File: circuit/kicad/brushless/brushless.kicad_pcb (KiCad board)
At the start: 2 copper layers, 52.3 x 51.5 mm, 20 parts, among them J1 MOTOR_OUTPUT, J2 POWER_INPUT, Q1 IRF540N, Q2 IRF540N, Q3 IRF540N

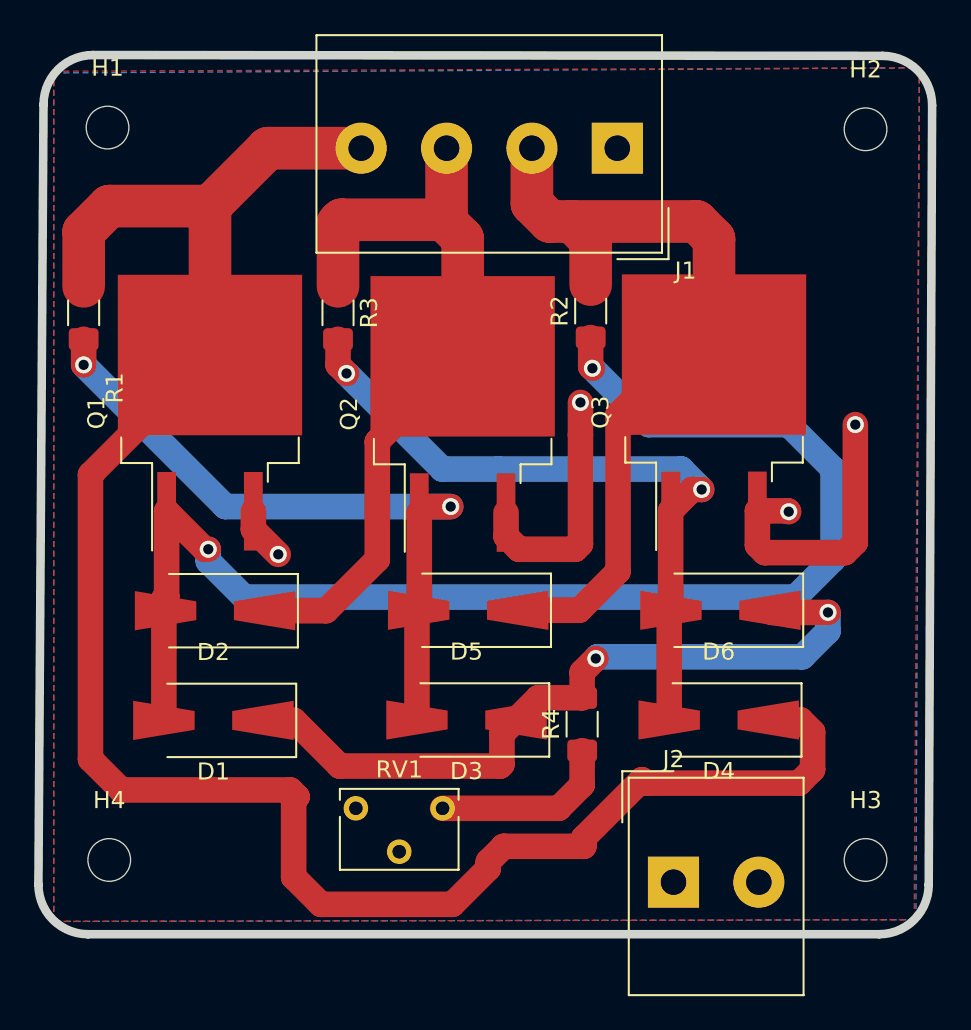
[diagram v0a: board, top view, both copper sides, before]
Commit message: UVW BLDC Example
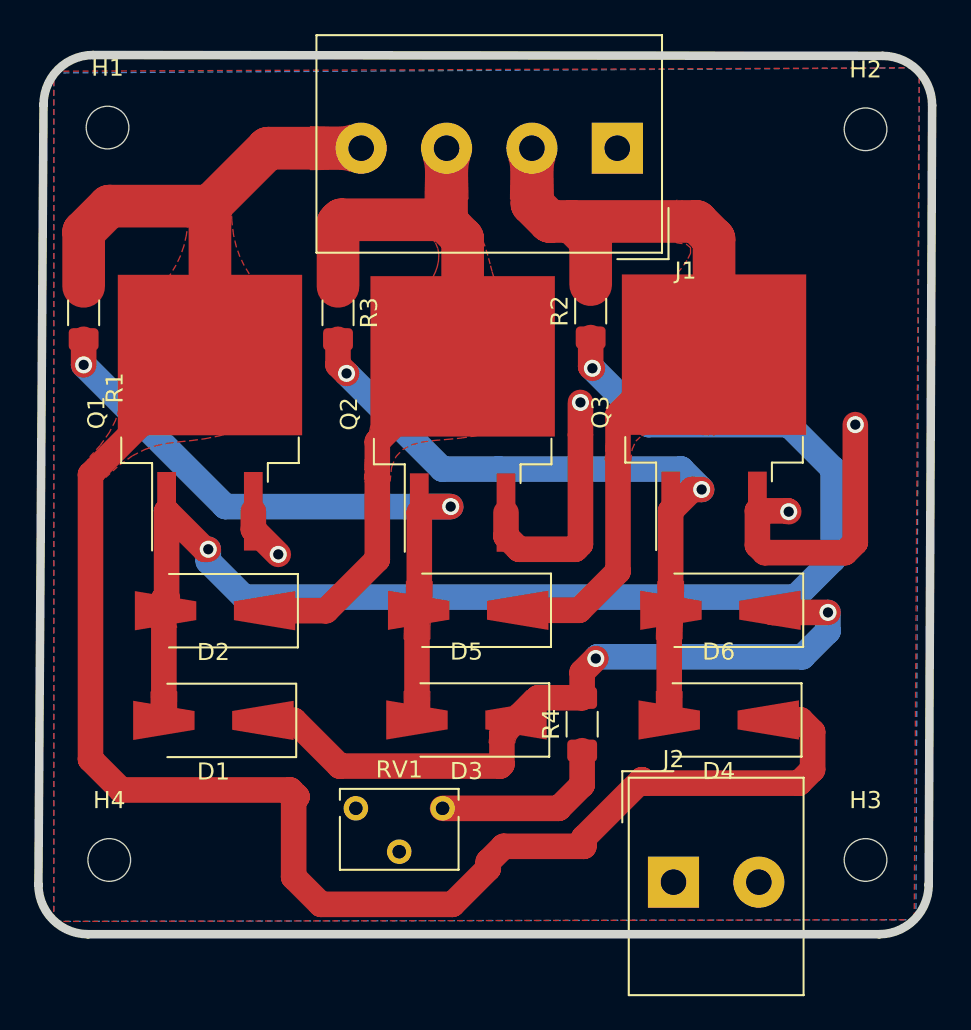
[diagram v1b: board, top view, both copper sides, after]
